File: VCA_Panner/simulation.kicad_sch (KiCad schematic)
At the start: 38 parts, among them U4 TL074, U5 TL074

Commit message: almost working
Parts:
- removed C10, C11, C12, C13, C8, C9: 47pF, symbol Device:C
- removed D3, D4: D, symbol Device:D
- removed R37, R39: 51k, symbol Device:R
- removed R38, R40: 4.7M, symbol Device:R
- removed R41, R42: 10k, symbol Device:R
- removed R43: 1k, symbol Device:R
- removed U4, U5: TL074, symbol Amplifier_Operational:TL074
- removed V3: VSIN, symbol Simulation_SPICE:VSIN
- added D1, D2: D, symbol Device:D
- added R1, R17: 20k, symbol Device:R
- added R10, R2: 99900, symbol Device:R
- added R11, R16, R18, R3, R4, R5, R7: 100k, symbol Device:R
- added R12, R13: 100, symbol Device:R
- added R14, R15: 730k, symbol Device:R
- added R6: 51k, symbol Device:R
- added R8: 56k, symbol Device:R
- added R9: 10k, symbol Device:R
- added U1, U2, U3: TL074, symbol Amplifier_Operational:TL074
- added V1: VSIN, symbol Simulation_SPICE:VSIN
- R19: value 10k -> 1k
- R20: value 10k -> 51k
- R21: value 10k -> 100k
- R22: value 10k -> 56k
- R23: value 9k -> 10k
- R25: value 1k -> 10k
- R26: value 9k -> 56k
- R27: value 1 -> 56k
- R28: value 99999 -> 10k
- R29, R30: value 100k -> 90k
- R31, R32: value 100k -> 56k
- R33, R34: value 51k -> 10k
- R35, R36: value 100k -> 10k
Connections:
- net +12V: now also R14.2, R15.2, U1.4 (V+), U2.4 (V+), U3.4 (V+); no longer R19.2, R21.2
- net -12V: now also U1.11 (V-), U2.11 (V-), U3.11 (V-); no longer R20.1, R22.1
- net GND: now also R29.1, R30.1, R10.1, R2.1, U1.10 (+), U1.3 (+), U1.5 (+), U2.10 (+), U2.3 (+), U2.5 (+), U3.10 (+), U3.12 (+), U3.3 (+), U3.5 (+), V1.2; no longer R28.2
- net out1: now also R19.1
- net out2: now also R24.1
- net at R31.1: now also R34.2, U3.6 (-)
- net at R31.2: now also R32.1, U3.1; no longer R29.1
- net at R32.2: now also R33.1, U3.2 (-); no longer R30.1
- net at R23.1: now also R25.2, U2.14; no longer R19.1
- net at R20.2: now also R16.1, U2.1; no longer R24.2
- net at R25.1: now also R26.2, U3.9 (-); no longer R21.1
- net at R27.2: now also R26.1, U3.8
- net at R29.2: now also R36.1, D2.2 (A)
- net at R35.1: now also R30.2, D2.1 (K), V1.1
- net at R34.1: now also R19.2, U3.7; no longer R36.2
- net at R22.2: now also R21.1, U2.8; no longer R26.2
- net at R35.2: now also D1.2 (A); no longer R33.1
- net at R27.1: now also R28.2, U3.13 (-); no longer R28.1
- new net: R5.1, U1.7
- new net: R4.1, R5.2, U1.6 (-)
- new net: R20.1, R21.2, U2.9 (-)
- new net: R7.1, R8.2, U1.8
- new net: R6.1, R7.2, U1.9 (-)
- new net: R10.2, R12.1, U1.12 (+)
- new net: R12.2, R15.1
- new net: R13.1, R2.2, U2.12 (+)
- new net: R13.2, R14.1
- new net: R16.2, R17.1, U2.2 (-)
- new net: R24.2, R28.1, U3.14
- new net: R22.1, R23.2, U2.13 (-)
- new net: R3.1, R6.2, U1.1
- new net: R1.1, R3.2, U1.2 (-)
- new net: D1.1 (K), R1.2
- new net: R33.2, R9.1, U1.14
- new net: R8.1, R9.2, U1.13 (-)
- new net: R11.1, R18.2, U2.6 (-)
- new net: R17.2, R18.1, U2.7
- new net: R11.2, R36.2
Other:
- moved on the sheet: V1, V2

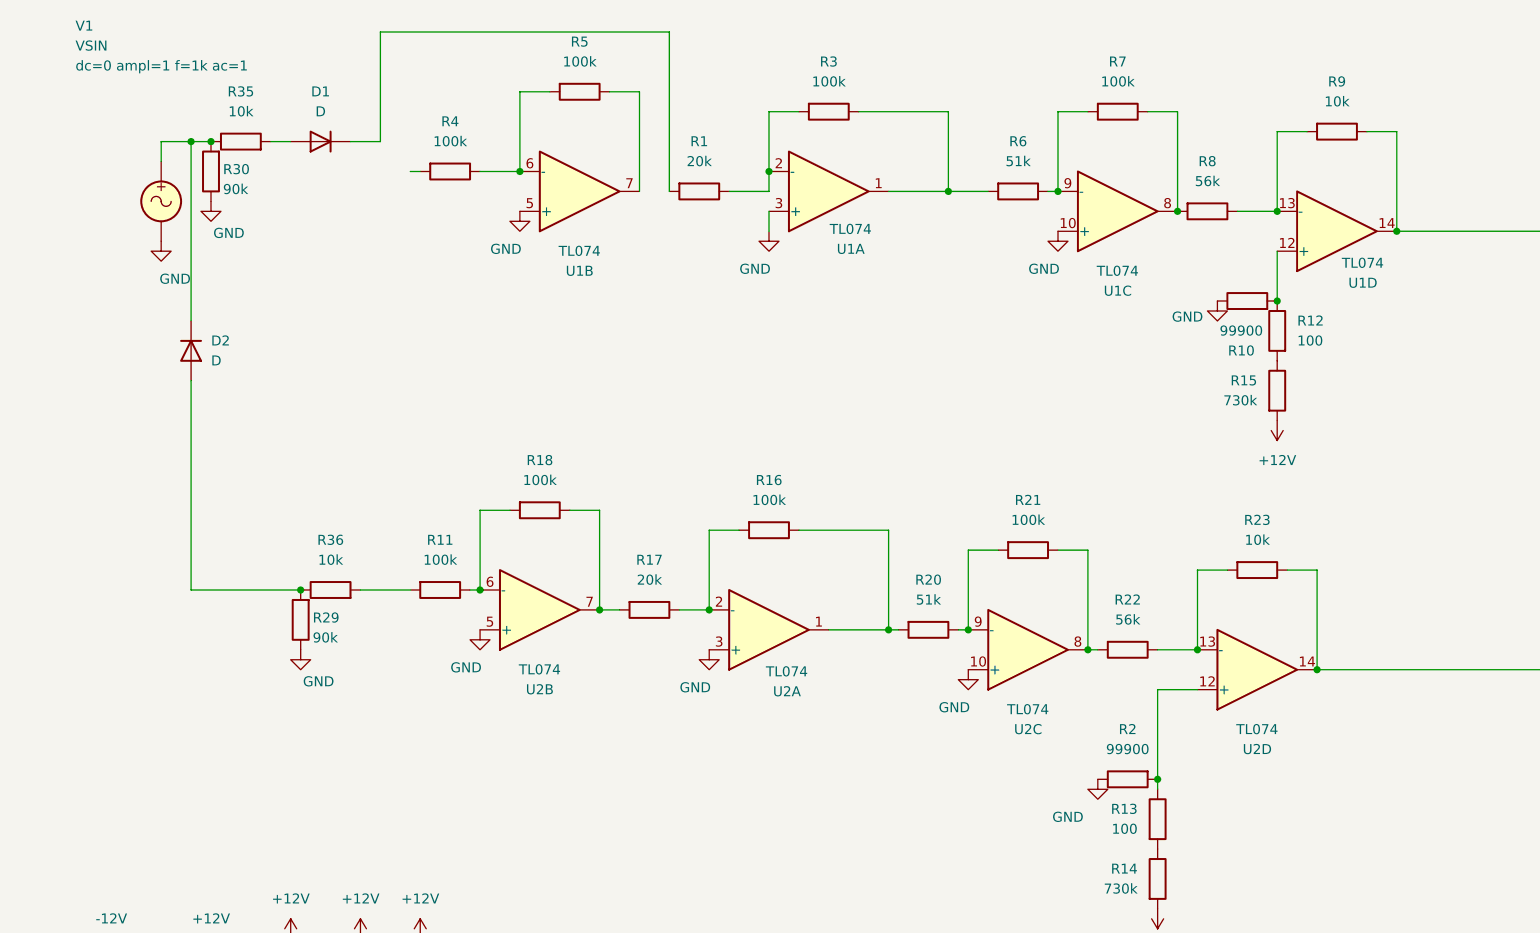
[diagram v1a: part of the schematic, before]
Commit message: added attenuverter
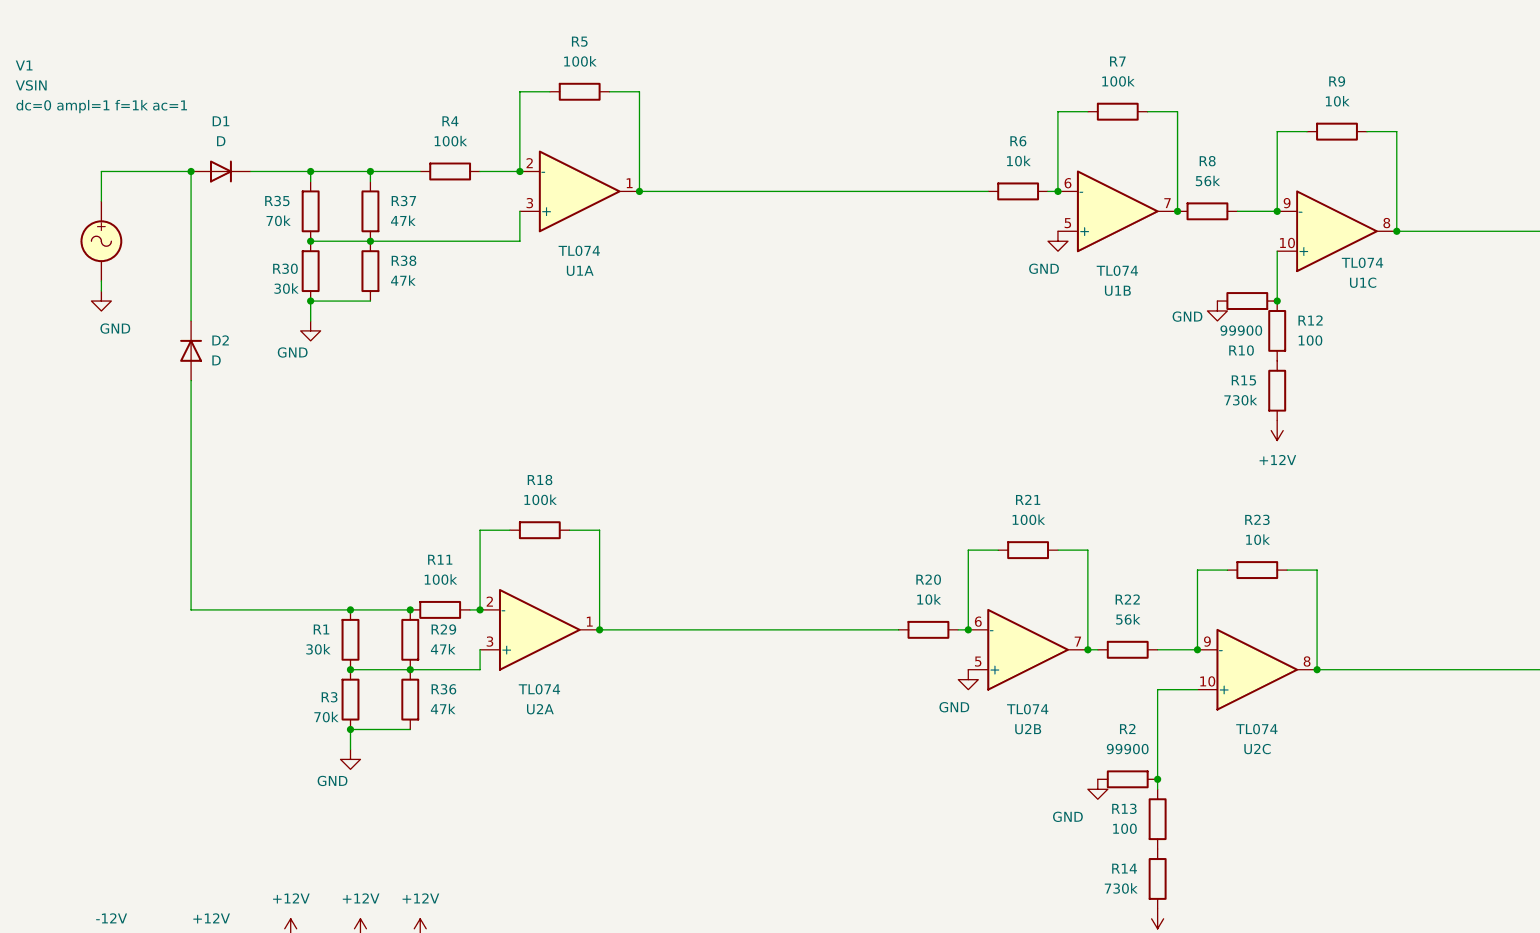
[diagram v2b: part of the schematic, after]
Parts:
- removed R16: 100k, symbol Device:R
- removed R17: 20k, symbol Device:R
- removed unit 1 of U1
- removed unit 1 of U2
- added R37, R38: 47k, symbol Device:R
- R1: value 20k -> 30k
- R20, R6: value 51k -> 10k
- R29: value 90k -> 47k
- R3: value 100k -> 70k
- R30: value 90k -> 30k
- R35: value 10k -> 70k
- R36: value 10k -> 47k
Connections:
- net GND: now also R3.1, R36.2, U1.5 (+), U2.5 (+), R38.2; no longer R29.1, U1.10 (+), U1.5 (+), U2.10 (+), U2.5 (+)
- net at R5.1: now also R6.2, U1.1; no longer U1.7
- net at R4.1, R5.2: now also U1.2 (-); no longer U1.6 (-)
- net at R20.1, R21.2: now also U2.6 (-); no longer U2.9 (-)
- net at R20.2: now also R18.1, U2.1
- net at R7.1, R8.2: now also U1.7; no longer U1.8
- net at R6.1, R7.2: now also U1.6 (-); no longer U1.9 (-)
- net at R10.2, R12.1: now also U1.10 (+); no longer U1.12 (+)
- net at R13.1, R2.2: now also U2.10 (+); no longer U2.12 (+)
- net at R22.1, R23.2: now also U2.9 (-); no longer U2.13 (-)
- net at R23.1, R25.2: now also U2.8; no longer U2.14
- net at R1.1, R3.2: now also R29.2, R36.1, U2.3 (+)
- net at R30.2, R35.1: now also U1.3 (+), R37.2, R38.1; no longer D2.1 (K), V1.1
- net at D1.1 (K): now also R35.2, R4.2, R37.1; no longer R1.2
- net at R33.2, R9.1: now also U1.8; no longer U1.14
- net at R8.1, R9.2: now also U1.9 (-); no longer U1.13 (-)
- net at R21.1, R22.2: now also U2.7; no longer U2.8
- net at R11.1, R18.2: now also U2.2 (-); no longer U2.6 (-)
- net at R11.2: now also D2.2 (A), R1.2, R29.1; no longer R36.2
- net at D1.2 (A): now also D2.1 (K), V1.1; no longer R35.2
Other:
- moved on the sheet: D1, R11, R18, U2A, V1

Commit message: finished schematic
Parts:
- R10, R2: value 99900 -> 100
- R12, R13: value 100 -> 99900
- R30: value 30k -> 100
- R35: value 70k -> 99900
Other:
- moved on the sheet: R10, R12, R15, R19, R31, R32, R33, R34, R5, R6, R7, R8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
